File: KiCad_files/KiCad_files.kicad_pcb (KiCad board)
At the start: 2 copper layers, 82 x 102 mm, 74 parts, among them J1 Conn_01x02_Socket, J2 L717HDE15P, J3 Conn_01x03_Socket, SW1 WE430182070816, U1 LM22670QMR-5.0, U2 MC33275ST-3.3T3G, U3 ADM3488ExR, U6 LT1789

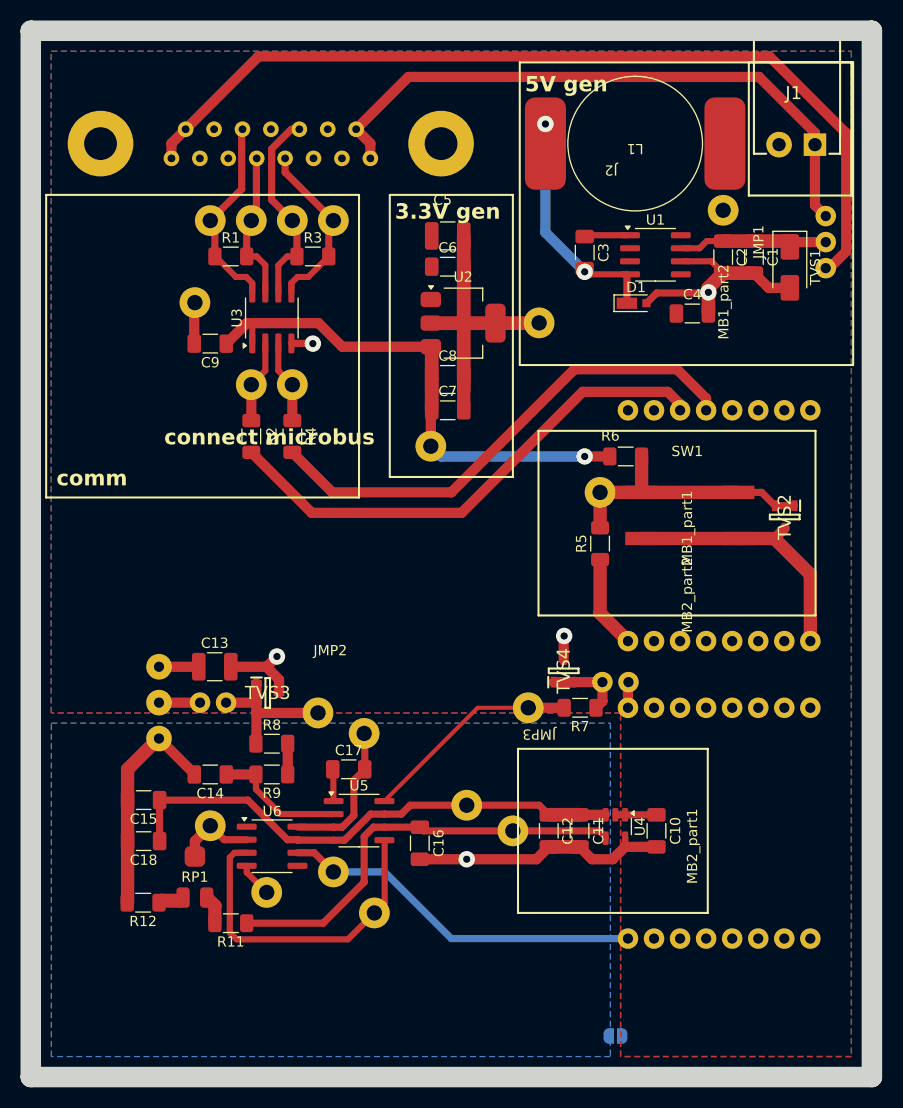
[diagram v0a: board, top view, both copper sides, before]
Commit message: Minor changes to the PCB and added a problems list
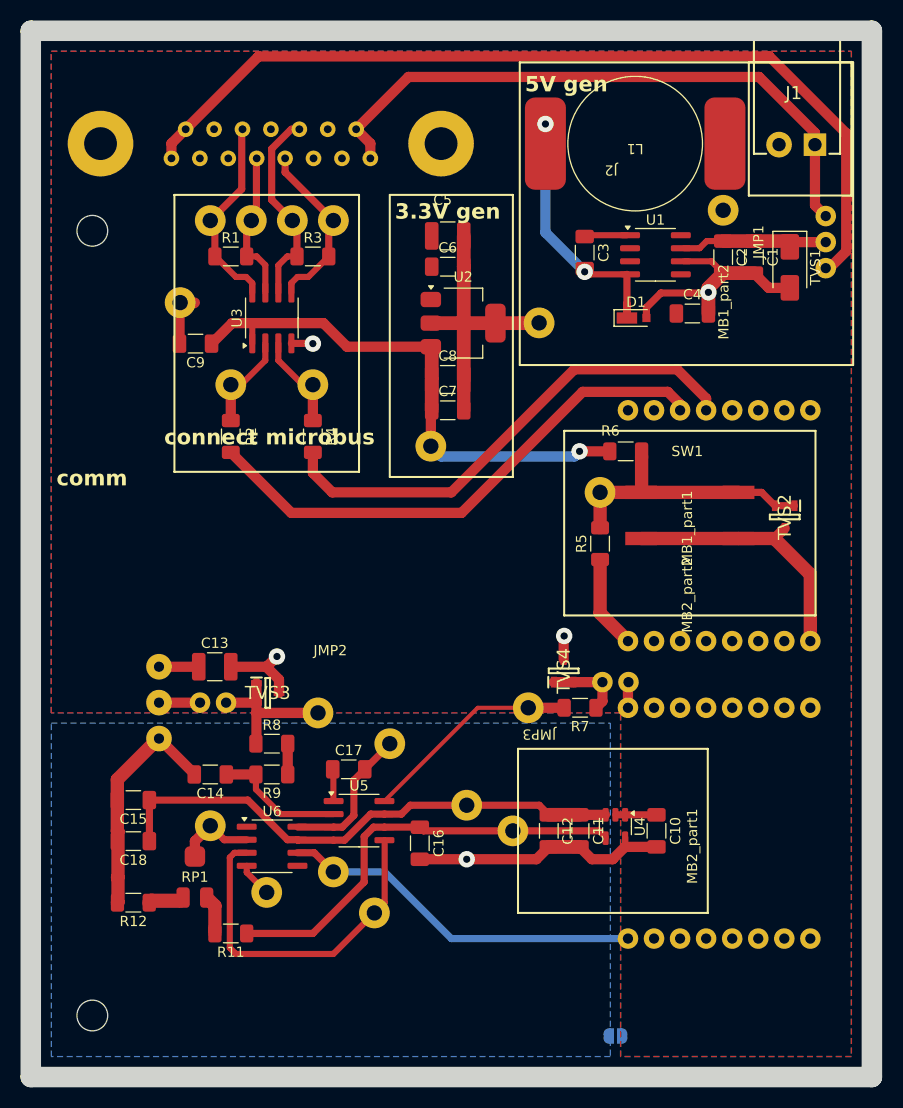
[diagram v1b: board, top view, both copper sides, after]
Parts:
- moved TP16 2.69 mm to (154.0, 108.5)
- moved R2 2.00 mm to (138.5, 78.5)
- moved R4 2.00 mm to (146.5, 78.5)
- moved TP5 2.00 mm to (138.5, 73.5)
- moved TP8 2.00 mm to (146.5, 73.5)
- moved C9 1.44 mm to (135.1, 69.5)
- moved D1 1.44 mm to (178.0, 67.0)
- moved TG2 1.44 mm to (133.6, 65.5)
- moved C15 1.00 mm to (129.0, 114.0)
- moved C18 1.00 mm to (129.0, 118.0)
- moved R11 1.00 mm to (138.5, 127.0)
- moved R12 0.95 mm to (129.0, 124.0)
- moved R6 0.50 mm to (177.0, 80.0)
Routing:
- net Net-(D1-K): track 23.2 -> 26.0 mm
- net Net-(U3-RO): track 7.38 -> 9.50 mm
- net Net-(U3-DI): track 7.38 -> 9.50 mm
- net Net-(U5-out): track 32.1 -> 34.2 mm
- net /MB1_14: track 50.2 -> 52.2 mm
- net +3.3V: track 51.2 -> 52.8 mm
- net Net-(RP1-CW): track 1.79 -> 3.04 mm
- net GNDD: track 94.4 -> 95.6 mm
- net Net-(RP1-CCW): track 2.83 -> 3.83 mm
- net +3.3VA: track 50.8 -> 51.8 mm
- net /MB1_13: track 49.3 -> 48.4 mm
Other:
- outline, holes or cut-outs redrawn
- board text added: "GPB24"
- board text removed: "Analog ground area"

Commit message: Forgot to save. Lol
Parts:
- added H1: MountingHole, MountingHole:MountingHole_3.2mm_M3, F.Cu at (125.0, 58.5)
- added H2: MountingHole, MountingHole:MountingHole_3.2mm_M3, F.Cu at (125.0, 135.0)
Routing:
- net GNDA: vias 1 -> 2
- added copper zone on F.Cu, net GNDA
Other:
- outline, holes or cut-outs redrawn

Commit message: Unremarkable changes
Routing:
- net /MB1_14: track 52.2 -> 54.9 mm
- net /MB1_13: track 48.4 -> 50.3 mm
- net /15: track 88.0 -> 87.2 mm
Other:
- board size 82 x 102 mm -> 80 x 100 mm
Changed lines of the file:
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@@
 	)
 	(gr_line
-		(start 201 141)
-		(end 201 39)
+		(start 200 140)
+		(end 200 40)
 		(stroke
 			(width 0.05)
@@
 	)
 	(gr_line
-		(start 119 39)
-		(end 119 141)
+		(start 120 40)
+		(end 120 140)
 		(stroke
 			(width 0.05)
@@
 	)
 	(gr_line
-		(start 201 141)
-		(end 119 141)
+		(start 200 140)
+		(end 120 140)
 		(stroke
 			(width 0.05)
@@
 	)
 	(gr_line
-		(start 119 39)
-		(end 201 39)
+		(start 120 40)
+		(end 200 40)
 		(stroke
 			(width 0.05)
@@
 	)
 	(segment
+		(start 198.5 60.5)
+		(end 198.5 49)
+		(width 1)
+		(layer "F.Cu")
+		(net 9)
+	)
+	(segment
+		(start 192 42.5)
+		(end 140.2 42.5)
+		(width 1)
+		(layer "F.Cu")
+		(net 9)
+	)
+	(segment
+		(start 132.715 49.985)
+		(end 132.715 51.44)
+		(width 1)
+		(layer "F.Cu")
+		(net 9)
+	)
+	(segment
+		(start 140.2 42.5)
+		(end 134.1 48.6)
+		(width 1)
+		(layer "F.Cu")
+		(net 9)
+	)
+	(segment
+		(start 196.8575 62.1425)
+		(end 198.5 60.5)
+		(width 1)
+		(layer "F.Cu")
+		(net 9)
+	)
+	(segment
+		(start 198.5 49)
+		(end 192 42.5)
+		(width 1)
+		(layer "F.Cu")
+		(net 9)
+	)
+	(segment
+		(start 134.1 48.6)
+		(end 132.715 49.985)
+		(width 1)
+		(layer "F.Cu")
+		(net 9)
+	)
+	(segment
 		(start 196.5 62.1425)
 		(end 196.8575 62.1425)
@@
 	)
 	(segment
-		(start 132.715 49.985)
-		(end 132.715 51.44)
-		(width 1)
-		(layer "F.Cu")
-		(net 9)
-	)
-	(segment
-		(start 196.8575 62.1425)
-		(end 198.5 60.5)
-		(width 1)
-		(layer "F.Cu")
-		(net 9)
-	)
-	(segment
-		(start 141.2 41.5)
-		(end 134.1 48.6)
-		(width 1)
-		(layer "F.Cu")
-		(net 9)
-	)
-	(segment
-		(start 198.5 49)
-		(end 191 41.5)
-		(width 1)
-		(layer "F.Cu")
-		(net 9)
-	)
-	(segment
-		(start 134.1 48.6)
-		(end 132.715 49.985)
-		(width 1)
-		(layer "F.Cu")
-		(net 9)
-	)
-	(segment
-		(start 198.5 60.5)
-		(end 198.5 49)
-		(width 1)
-		(layer "F.Cu")
-		(net 9)
-	)
-	(segment
-		(start 191 41.5)
-		(end 141.2 41.5)
-		(width 1)
-		(layer "F.Cu")
-		(net 9)
-	)
-	(segment
 		(start 146.05 63)
 		(end 148.05 61)
@@
 	)
 	(segment
+		(start 144.5 57.5)
+		(end 142.483 55.483)
+		(width 0.7)
+		(layer "F.Cu")
+		(net 12)
+	)
+	(segment
+		(start 142.483 50.517)
+		(end 144.4 48.6)
+		(width 0.7)
+		(layer "F.Cu")
+		(net 12)
+	)
+	(segment
+		(start 144.95 61)
+		(end 144.95 57.95)
+		(width 0.7)
+		(layer "F.Cu")
+		(net 12)
+	)
+	(segment
+		(start 144 61)
+		(end 144.95 61)
+		(width 0.6)
+		(layer "F.Cu")
+		(net 12)
+	)
+	(segment
+		(start 144.4 48.6)
+		(end 145.18 48.6)
+		(width 0.7)
+		(layer "F.Cu")
+		(net 12)
+	)
+	(segment
+		(start 144.95 57.95)
+		(end 144.5 57.5)
+		(width 0.7)
+		(layer "F.Cu")
+		(net 12)
+	)
+	(segment
 		(start 142.483 55.483)
 		(end 142.483 50.517)
@@
 	)
 	(segment
-		(start 144.95 61)
-		(end 144.95 57.95)
-		(width 0.7)
-		(layer "F.Cu")
-		(net 12)
-	)
-	(segment
-		(start 144 61)
-		(end 144.95 61)
-		(width 0.6)
-		(layer "F.Cu")
-		(net 12)
-	)
-	(segment
-		(start 142.483 50.517)
-		(end 144.4 48.6)
-		(width 0.7)
-		(layer "F.Cu")
-		(net 12)
-	)
-	(segment
-		(start 144.95 57.95)
-		(end 144.5 57.5)
-		(width 0.7)
-		(layer "F.Cu")
-		(net 12)
-	)
-	(segment
 		(start 143.135 64.525)
 		(end 143.135 61.865)
@@
 	)
 	(segment
-		(start 144.5 57.5)
-		(end 142.483 55.483)
-		(width 0.7)
-		(layer "F.Cu")
-		(net 12)
-	)
-	(segment
-		(start 144.4 48.6)
-		(end 145.18 48.6)
-		(width 0.7)
-		(layer "F.Cu")
-		(net 12)
-	)
-	(segment
 		(start 143.135 61.865)
 		(end 144 61)
@@
 	)
 	(segment
+		(start 190.5 44)
+		(end 155.32 44)
+		(width 1)
+		(layer "F.Cu")
+		(net 13)
+	)
+	(segment
 		(start 150.72 48.6)
 		(end 152.105 49.985)
@@
 	)
 	(segment
-		(start 195.45 48.95)
-		(end 190 43.5)
-		(width 1)
-		(layer "F.Cu")
-		(net 13)
-	)
-	(segment
 		(start 195.45 50.1)
 		(end 195.45 48.95)
@@
 	)
 	(segment
-		(start 195.45 56.0125)
+		(start 155.32 44)
+		(end 150.72 48.6)
+		(width 1)
+		(layer "F.Cu")
+		(net 13)
+	)
+	(segment
+		(start 195.45 50.1)
+		(end 196.1 50.1)
+		(width 1)
+		(layer "F.Cu")
+		(net 13)
+	)
+	(segment
+		(start 195.45 48.95)
+		(end 190.5 44)
+		(width 1)
+		(layer "F.Cu")
+		(net 13)
+	)
+	(segment
+		(start 196.5 50.5)
 		(end 196.5 57.0625)
 		(width 1)
@@
 	)
 	(segment
-		(start 155.82 43.5)
-		(end 150.72 48.6)
-		(width 1)
-		(layer "F.Cu")
-		(net 13)
-	)
-	(segment
-		(start 195.45 50.1)
-		(end 195.45 56.0125)
-		(width 1)
-		(layer "F.Cu")
-		(net 13)
-	)
-	(segment
-		(start 190 43.5)
-		(end 155.82 43.5)
+		(start 196.1 50.1)
+		(end 196.5 50.5)
 		(width 1)
 		(layer "F.Cu")
@@
 	)
 	(segment
-		(start 161 86)
-		(end 172.8 74.2)
+		(start 160 86)
+		(end 173.5 72.5)
 		(width 1)
 		(layer "F.Cu")
@@
 	)
 	(segment
-		(start 182.3 75.4)
+		(start 181.5 72.5)
+		(end 182.3 73.3)
+		(width 1)
+		(layer "F.Cu")
+		(net 26)
+	)
+	(segment
+		(start 182.3 73.3)
 		(end 182.3 76)
 		(width 1)
@@
 	)
 	(segment
-		(start 144.4 86)
-		(end 161 86)
+		(start 173.5 72.5)
+		(end 181.5 72.5)
 		(width 1)
 		(layer "F.Cu")
@@
 	)
 	(segment
-		(start 181.1 74.2)
-		(end 182.3 75.4)
+		(start 144.4 86)
+		(end 160 86)
 		(width 1)
 		(layer "F.Cu")
@@
 	)
 	(segment
-		(start 172.8 74.2)
-		(end 181.1 74.2)
-		(width 1)
-		(layer "F.Cu")
-		(net 26)
-	)
-	(segment
-		(start 172 72)
-		(end 182 72)
+		(start 148.9 84.5)
+		(end 159.5 84.5)
 		(width 1)
 		(layer "F.Cu")
@@
 	)
 	(segment
-		(start 182 72)
-		(end 184.84 74.84)
+		(start 182 71)
+		(end 184.84 73.84)
 		(width 1)
 		(layer "F.Cu")
@@
 	)
 	(segment
+		(start 184.84 73.84)
+		(end 184.84 76)
+		(width 1)
+		(layer "F.Cu")
+		(net 27)
+	)
+	(segment
+		(start 159.5 84.5)
+		(end 173 71)
+		(width 1)
+		(layer "F.Cu")
+		(net 27)
+	)
+	(segment
+		(start 173 71)
+		(end 182 71)
+		(width 1)
+		(layer "F.Cu")
+		(net 27)
+	)
+	(segment
 		(start 146.5 82.1)
-		(end 148.4 84)
-		(width 1)
-		(layer "F.Cu")
-		(net 27)
-	)
-	(segment
-		(start 184.84 74.84)
-		(end 184.84 76)
+		(end 148.9 84.5)
 		(width 1)
 		(layer "F.Cu")
@@
 		(start 146.5 80.1)
 		(end 146.5 82.1)
-		(width 1)
-		(layer "F.Cu")
-		(net 27)
-	)
-	(segment
-		(start 160 84)
-		(end 172 72)
-		(width 1)
-		(layer "F.Cu")
-		(net 27)
-	)
-	(segment
-		(start 148.4 84)
-		(end 160 84)
 		(width 1)
 		(layer "F.Cu")
@@
 		(layer "F.Cu")
 		(net 55)
-	)
-	(segment
-		(start 134.9375 65.5625)
-		(end 135 65.5)
-		(width 1)
-		(layer "F.Cu")
-		(net 55)

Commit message: Fixed all 'problems'
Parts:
- C12: footprint Capacitor_SMD:C_1206_3216Metric_Pad1.33x1.80mm_HandSolder -> Capacitor_SMD:C_1210_3225Metric_Pad1.33x2.70mm_HandSolder
- C4: value 10nF -> 10uF; footprint Capacitor_SMD:C_1206_3216Metric_Pad1.33x1.80mm_HandSolder -> Capacitor_SMD:C_1210_3225Metric_Pad1.33x2.70mm_HandSolder
- U1: footprint Package_SO:SOIC-8_3.9x4.9mm_P1.27mm -> Package_SO:SOIC-8-1EP_3.9x4.9mm_P1.27mm_EP2.41x3.81mm
- moved D1 9.73 mm to (183.7, 59.1)
- moved C10 5.80 mm to (175.9, 121.1), turned to 180 degrees
- moved TP1 5.47 mm to (191.9, 55.6)
- moved C4 5.06 mm to (187.3, 69.9), turned to 90 degrees
- moved C2 4.28 mm to (183.7, 64.3)
- moved C12 4.27 mm to (167.2, 113.4), turned to 90 degrees
- moved C11 4.22 mm to (170.3, 113.4), turned to 90 degrees
- moved C1 3.91 mm to (187.3, 64.3)
- moved U1 3.84 mm to (177.4, 63.8)
- moved C3 3.82 mm to (176.5, 59.1), turned to 0 degrees
- moved J3 3.50 mm to (131.7, 101.0)
- moved U4 2.59 mm to (173.4, 116.5), turned to 90 degrees
- moved TVS1 2.49 mm to (191.9, 64.3)
- moved TP11 2.15 mm to (164.1, 118.0)
- moved TGA1 0.71 mm to (142.5, 123.5)
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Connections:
- J3 pad 2: Net-(J3-Pin_2) -> GNDA
- J3 pad 3: GNDA -> Net-(J3-Pin_2)
- U1 pad 4: Net-(D1-K) -> +5V
- U1 pad 8: +5V -> Net-(D1-K)
- U4 pad 1: +5V -> /VBIAS
- U4 pad 2: +5V -> GNDA
- U4 pad 3: +3.3VA -> +5V
- U4 pad 4: /VBIAS -> +5V
- U4 pad 5: GNDA -> +3.3VA
- U6 pad 5: unconnected-(U6-NC-Pad5) -> GNDA
- U6 pad 8: GNDA -> unconnected-(U6-NC-Pad8)
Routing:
- net GNDD: track 95.5 -> 150.9 mm, vias 4 -> 5
- net GNDA: track 66.4 -> 12.6 mm, vias 2 -> 0
- net Net-(TVS1-A1): track 14.5 -> 22.7 mm, vias 0 -> 1
- net +5V: track 12.5 -> 5.40 mm
- net Net-(D1-K): track 26.0 -> 30.2 mm
- net /VBIAS: track 42.8 -> 39.7 mm
- net +3.3VA: track 51.8 -> 49.1 mm
- net Net-(U1-BOOT): track 4.17 -> 2.72 mm
- net Net-(U5-out): track 34.2 -> 32.7 mm
- net +3.3V: track 52.8 -> 52.2 mm
- net /MB2_1: vias 0 -> 1

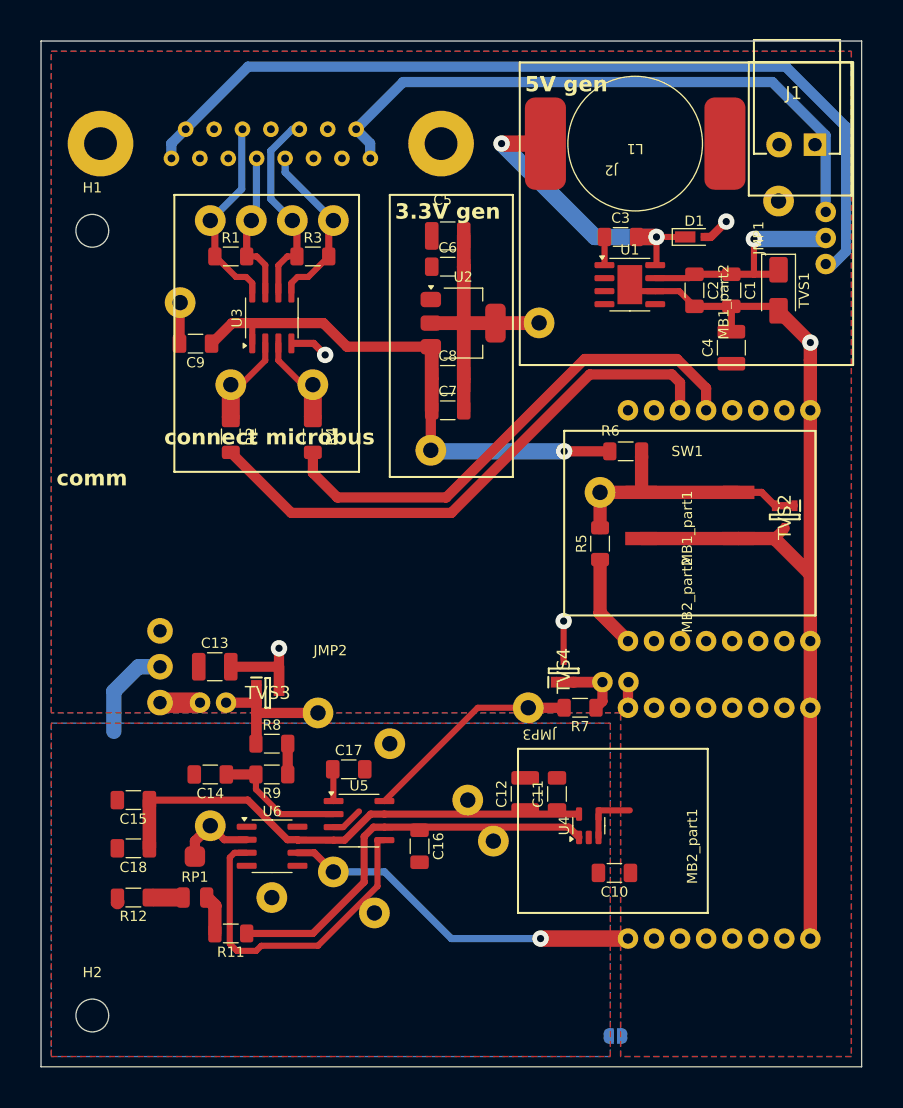
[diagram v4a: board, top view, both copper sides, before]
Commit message: Finalizing the PCB. Fixed mounting holes and flipped some components to the other side so jumpers can be soldered easily
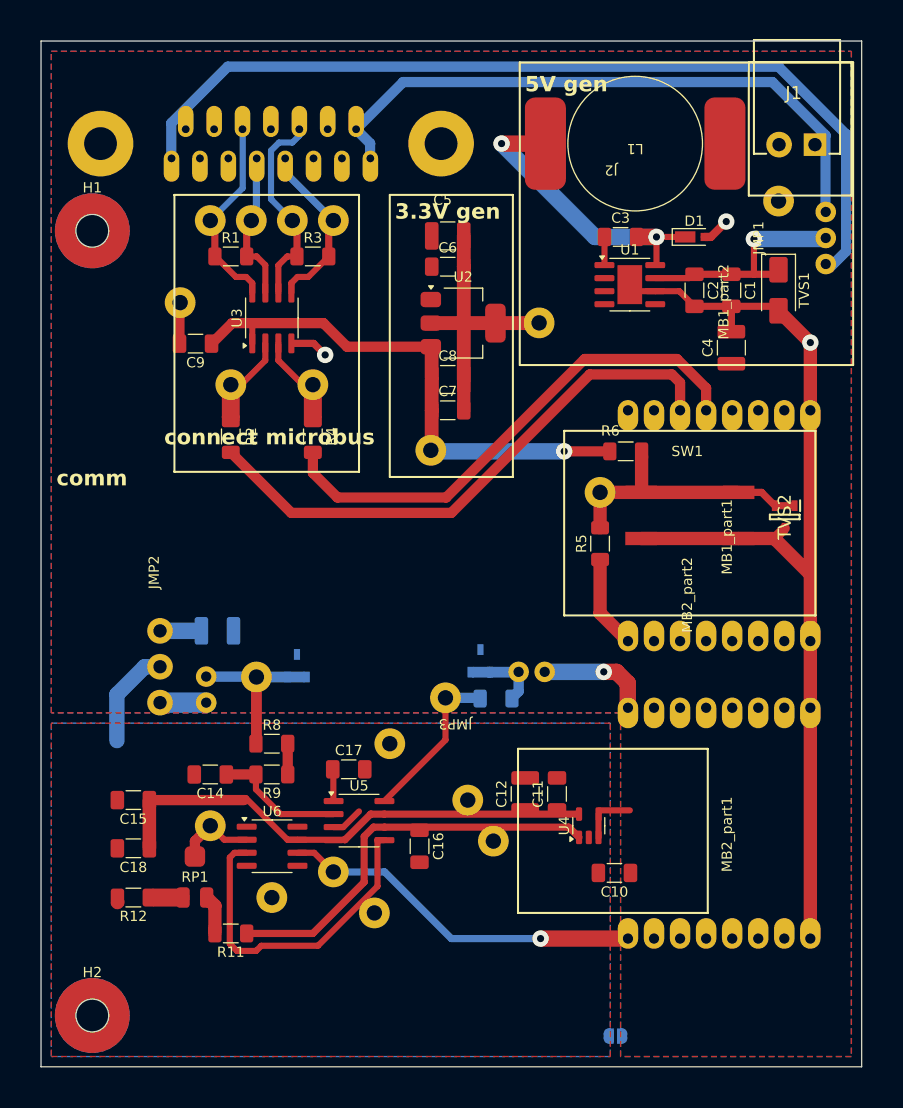
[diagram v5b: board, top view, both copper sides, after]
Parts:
- C13, R7, TVS3, TVS4: moved to B.Cu
- moved R7 8.24 mm to (164.4, 104.1)
- moved JMP3 8.23 mm to (169.1, 101.5)
- moved TVS4 8.18 mm to (162.8, 100.4)
- moved TP13 8.13 mm to (159.4, 104.0)
- moved TP12 6.95 mm to (141.0, 102.0)
- moved TVS3 3.89 mm to (144.9, 100.9), turned to 90 degrees
- moved C13 3.51 mm to (137.2, 97.5)
- moved JMP2 0.60 mm to (136.1, 104.5), turned to 90 degrees
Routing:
- net GNDD: track 150.9 -> 139.7 mm, vias 5 -> 3
- net /MB2_16: track 2.52 -> 11.0 mm, vias 0 -> 1
- net Net-(U5-clk): track 21.3 -> 16.9 mm
- net +5V: track 5.40 -> 9.20 mm
- net Net-(TVS3-CATHODE_COMPENSATION_DIODE): track 14.6 -> 15.9 mm
- net /11: track 19.8 -> 21.1 mm
- net /15: track 87.6 -> 88.3 mm
- net Net-(J3-Pin_2): track 4.00 -> 4.60 mm
